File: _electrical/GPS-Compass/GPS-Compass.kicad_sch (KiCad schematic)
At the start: 116 parts, among them J1 Conn_01x02_Pin, J2 USB_TypeC, J3 01x10, J4 01x10, J5 Conn_01x02_Pin, J6 FFC2B28-12-G, Q1 SI2393DS, SW1 SHIP-MODE, SW2 RST, SW3 RESET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

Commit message: IMU test
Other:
- note added: "I2C Addr.: 0x25"
- note added: "I2C Addr.: 0x28"
- note added: "I2C Addr.: 0x6A"
- note removed: "1) Uvod 2) Obsah 3) Koncept 4-7) Popis realizace 8) Zaver - splneni veci"
- note removed: "https://cz.mouser.com/ProductDetail/Texas-Instruments/BQ25895MRTWR?qs=uNh9J9Y3wTe%2F%252BmcQbu7CLA%3D%3D"
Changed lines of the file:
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@@
-		)
-	)
-	(text "1) Uvod\n2) Obsah\n3) Koncept\n4-7) Popis realizace\n8) Zaver - splneni veci"
-		(exclude_from_sim no)
-		(at 494.665 294.64 0)
-		(effects
-			(font
-				(size 3 3)
-			)
-			(justify left)
 		)
 	)
@@
 		)
 	)
+	(text "I2C Addr.: 0x28"
+		(exclude_from_sim no)
+		(at 151.765 250.19 0)
+		(effects
+			(font
+				(size 1.27 1.27)
+			)
+			(justify left bottom)
+		)
+	)
 	(text "MAIN SW"
 		(exclude_from_sim no)
@@
 		)
 	)
+	(text "I2C Addr.: 0x6A"
+		(exclude_from_sim no)
+		(at 114.935 149.225 0)
+		(effects
+			(font
+				(size 1.27 1.27)
+			)
+			(justify left bottom)
+		)
+	)
 	(text "MCU and IMU"
 		(exclude_from_sim no)
@@
 		)
 	)
-	(text "https://cz.mouser.com/ProductDetail/Texas-Instruments/BQ25895MRTWR?qs=uNh9J9Y3wTe%2F%252BmcQbu7CLA%3D%3D"
-		(exclude_from_sim no)
-		(at 581.66 146.685 0)
-		(effects
-			(font
-				(size 1.27 1.27)
-			)
-		)
-	)
 	(text "TESTING POINTS"
 		(exclude_from_sim no)
@@
 			)
 			(justify left bottom)
+		)
+	)
+	(text "I2C Addr.: 0x25"
+		(exclude_from_sim no)
+		(at 180.34 67.31 0)
+		(effects
+			(font
+				(size 1.27 1.27)
+			)
+			(justify left bottom)

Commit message: Code update, schematic plots, text update
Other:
- note added: "1. 2. 3. 4. 5. 6. 7."
- note added: "I2C ADDR."
- note added: "IMU: 0x28 EEPROM: 0x50 USB CTRL: 0x25 CHARGER: 0x6A"
- note removed: "1. Shift register pins check 2. UI pin pinout fix 3. 4. 5. STAT - charging in progress silkscreen 6. 7."
- note removed: "I2C ADRESS + GPIO TIES"
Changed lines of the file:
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@@
 		)
 	)
-	(text "I2C ADRESS + GPIO TIES"
+	(text "I2C ADDR."
 		(exclude_from_sim no)
 		(at 36.83 226.695 0)
@@
 		)
 	)
-	(text "1. Shift register pins check\n2. UI pin pinout fix\n3. \n4. \n5. STAT - charging in progress silkscreen\n6.\n7. "
+	(text "1. \n2. \n3. \n4. \n5. \n6.\n7. "
 		(exclude_from_sim no)
 		(at 19.685 307.975 0)
@@
 			)
 			(justify left bottom)
+		)
+	)
+	(text "IMU: 0x28\nEEPROM: 0x50\nUSB CTRL: 0x25\nCHARGER: 0x6A"
+		(exclude_from_sim no)
+		(at 38.1 241.3 0)
+		(effects
+			(font
+				(face "Bahnschrift")
+				(size 2 2)
+				(color 0 0 0 1)
+			)
+			(justify left bottom)

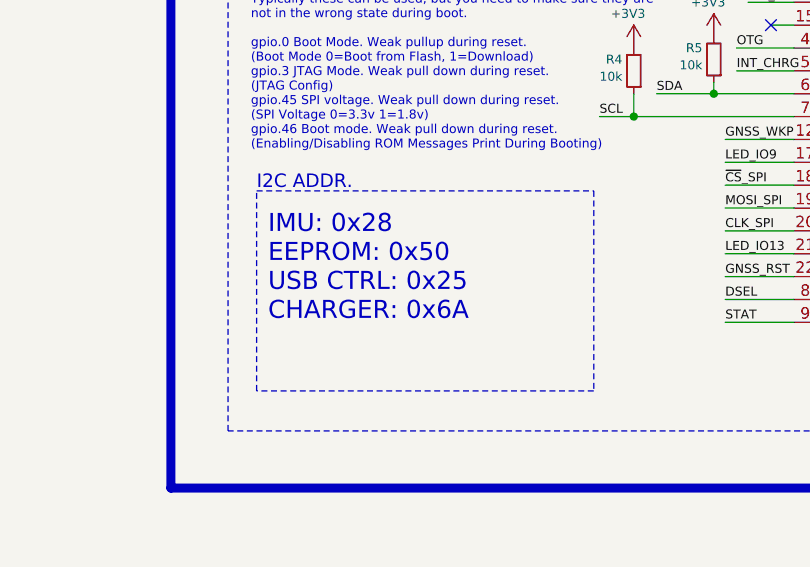
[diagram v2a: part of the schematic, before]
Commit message: I2C GNSS update
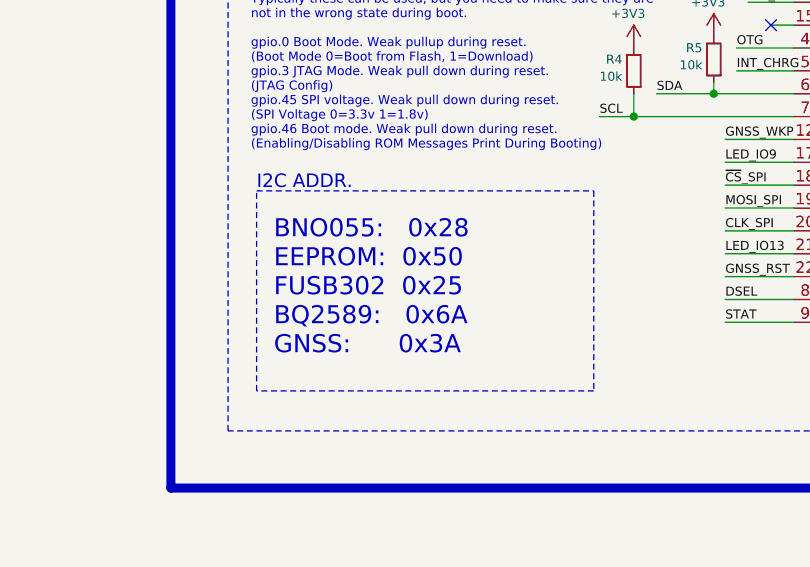
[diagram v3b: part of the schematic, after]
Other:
- note added: "BNO055: 0x28 EEPROM: 0x50 FUSB302 0x25 BQ2589: 0x6A GNSS: 0x3A"
- note removed: "IMU: 0x28 EEPROM: 0x50 USB CTRL: 0x25 CHARGER: 0x6A"
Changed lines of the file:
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@@
 		)
 	)
-	(text "IMU: 0x28\nEEPROM: 0x50\nUSB CTRL: 0x25\nCHARGER: 0x6A"
+	(text "BNO055:   0x28\nEEPROM:  0x50\nFUSB302  0x25\nBQ2589:   0x6A\nGNSS:      0x3A"
 		(exclude_from_sim no)
-		(at 38.1 241.3 0)
+		(at 38.735 245.11 0)
 		(effects
 			(font
